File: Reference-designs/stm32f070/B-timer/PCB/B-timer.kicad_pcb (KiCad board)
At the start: 2 copper layers, 65 x 45 mm, 121 parts, among them J1 USB_B_Micro, J2 Conn_02x05_Odd_Even, SW1 SW_Push, SW2 SW_Push, SW3 SW_Push, U1 STM32F070C6Tx, U2 MIC5504-3.3YM5

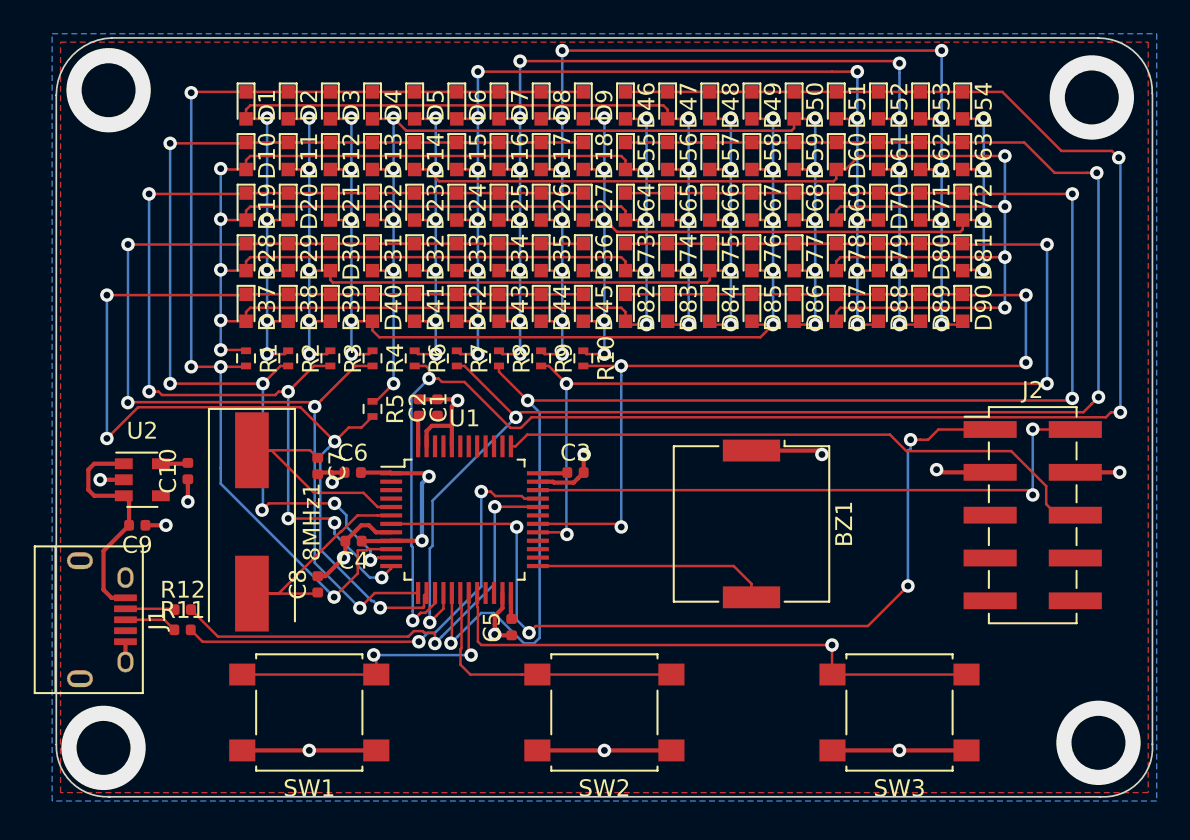
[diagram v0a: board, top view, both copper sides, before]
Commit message: Generated code for B-timer V2
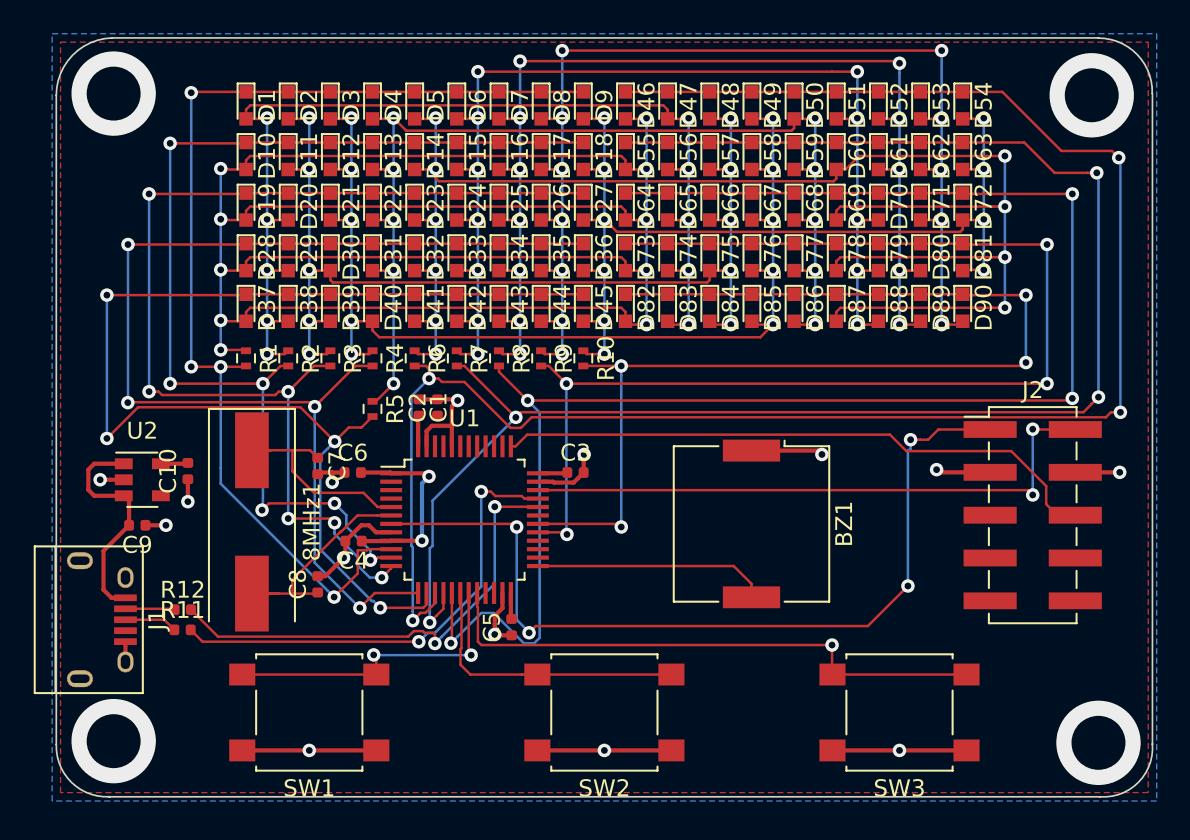
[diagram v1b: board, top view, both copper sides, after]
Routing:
- net Net-(8MHz1-Pad1): track 13.7 -> 13.2 mm

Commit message: Adjusted 68R and 18pF values and regenerated kicad_pcb file
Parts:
- C7, C8: value 0.1µF -> 18pF
- R1, R10, R2, R3, R4, R5, R6, R7, R8, R9: value R -> 68R
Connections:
- J1 pad 4: (no net) -> Net-(J1-Pad4)
- J2 pad 10: (no net) -> Net-(J2-Pad10)
- J2 pad 5: (no net) -> Net-(J2-Pad5)
- J2 pad 8: (no net) -> Net-(J2-Pad8)
- J2 pad 9: (no net) -> Net-(J2-Pad9)
- U1 pad 2: (no net) -> Net-(U1-Pad2)
- U1 pad 21: (no net) -> Net-(U1-Pad21)
- U1 pad 22: (no net) -> Net-(U1-Pad22)
- U1 pad 26: (no net) -> Net-(U1-Pad26)
- U1 pad 27: (no net) -> Net-(U1-Pad27)
- U1 pad 28: (no net) -> Net-(U1-Pad28)
- U1 pad 3: (no net) -> Net-(U1-Pad3)
- U1 pad 31: (no net) -> Net-(U1-Pad31)
- U1 pad 38: (no net) -> Net-(U1-Pad38)
- U1 pad 39: (no net) -> Net-(U1-Pad39)
- U1 pad 4: (no net) -> Net-(U1-Pad4)
- U1 pad 40: (no net) -> Net-(U1-Pad40)
- U1 pad 41: (no net) -> Net-(U1-Pad41)
- U1 pad 42: (no net) -> Net-(U1-Pad42)
- U1 pad 43: (no net) -> Net-(U1-Pad43)
- U1 pad 45: (no net) -> Net-(U1-Pad45)
- U1 pad 46: (no net) -> Net-(U1-Pad46)
- U2 pad 4: (no net) -> Net-(U2-Pad4)
